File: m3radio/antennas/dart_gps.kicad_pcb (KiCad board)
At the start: 2 copper layers, 138 x 93 mm, 5 parts

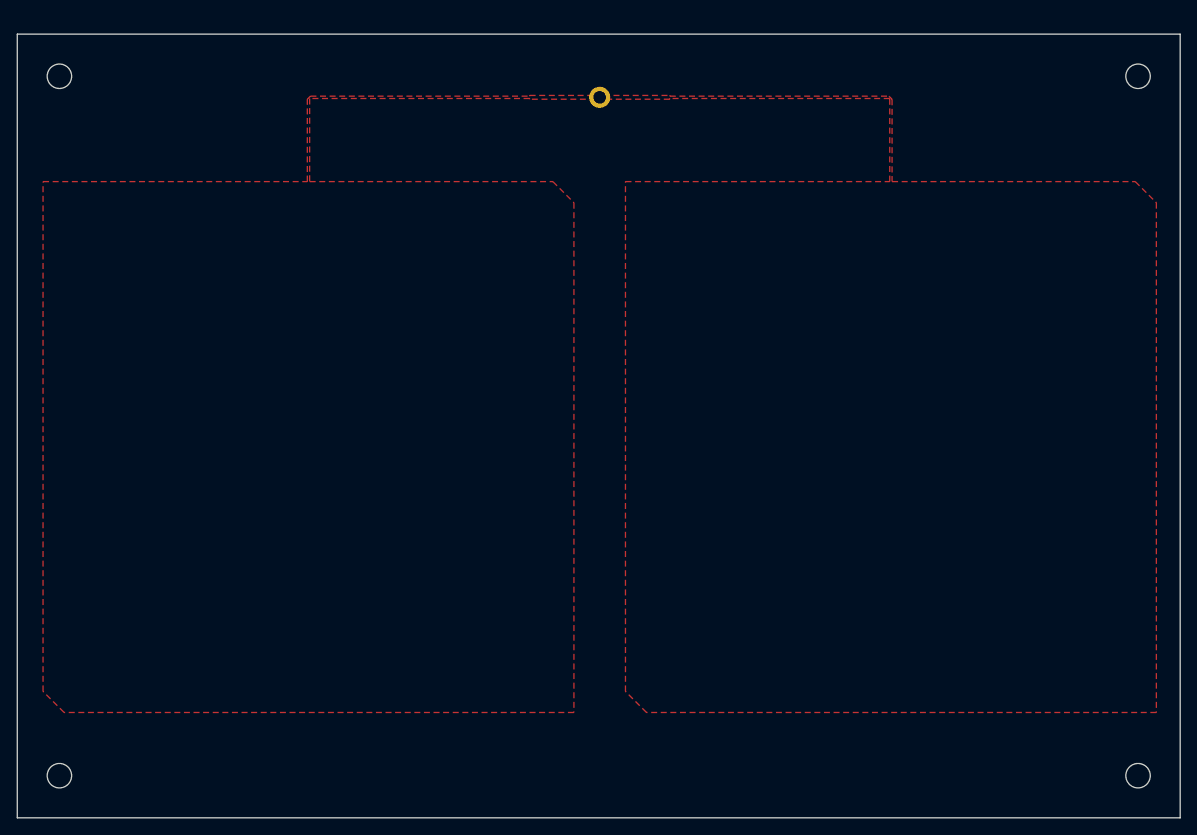
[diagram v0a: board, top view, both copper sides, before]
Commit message: make smaller dart antenna cutouts to ease manufacture
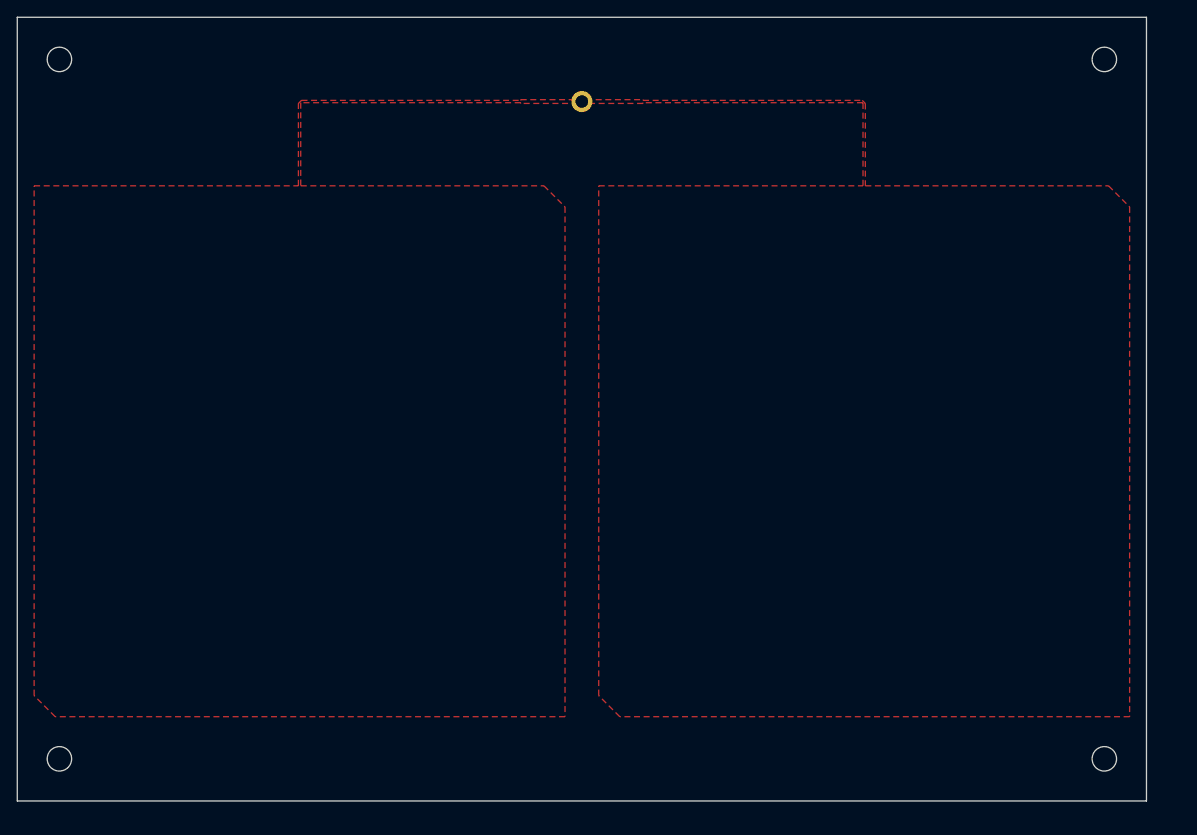
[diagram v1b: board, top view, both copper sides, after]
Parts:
- moved ? 4.47 mm to (149.0, 173.0)
- moved ? 4.47 mm to (149.0, 256.0)
- moved ? 2.17 mm to (87.0, 178.0)
- moved ? 2.00 mm to (25.0, 256.0)
- moved ? 2.00 mm to (25.0, 173.0)
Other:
- board size 138 x 93 mm -> 134 x 93 mm
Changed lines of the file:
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@@
-(kicad_pcb (version 20160815) (host pcbnew no-vcs-found-7520~57~ubuntu14.04.1)
+(kicad_pcb (version 20170123) (host pcbnew no-vcs-found-7587~57~ubuntu14.04.1)
   (general
-    (links 0)
-    (no_connects 0)
-    (area 19.949999 169.949999 158.050001 263.050001)
+    (links 1)
+    (no_connects 1)
+    (area 19.949999 167.949999 154.050001 261.050001)
     (thickness 1.6)
     (drawings 4)
@@
   (layers
     (0 F.Cu signal)
-    (31 B.Cu signal hide)
+    (31 B.Cu signal)
     (40 Dwgs.User user)
     (44 Edge.Cuts user)
@@
       (psnegative false)
       (psa4output false)
-      (plotreference true)
-      (plotvalue true)
+      (plotreference false)
+      (plotvalue false)
       (plotinvisibletext false)
       (padsonsilk false)
@@
   )
   (module X1 (layer F.Cu)
-    (at 153 175)
+    (at 87 178)
+    (fp_text reference "" (at 0 0) (layer F.SilkS)
+      (effects (font (thickness 0.15)))
+    )
+    (fp_text value "" (at 0 0) (layer F.SilkS)
+      (effects (font (thickness 0.15)))
+    )
+    (pad 1 thru_hole circle (at 0 0) (size 2.5 2.5) (drill 1.5) (layers F.Cu)
+      (net 1 Antennas) (zone_connect 2))
+  )
+  (module X1 (layer F.Cu)
+    (at 149 173)
     (fp_text reference "" (at 0 0) (layer F.SilkS)
       (effects (font (thickness 0.15)))
@@
   )
   (module X1 (layer F.Cu)
-    (at 153 258)
+    (at 149 256)
     (fp_text reference "" (at 0 0) (layer F.SilkS)
       (effects (font (thickness 0.15)))
@@
   )
   (module X1 (layer F.Cu)
-    (at 25 258)
+    (at 25 256)
     (fp_text reference "" (at 0 0) (layer F.SilkS)
       (effects (font (thickness 0.15)))
@@
   )
   (module X1 (layer F.Cu)
-    (at 25 175)
+    (at 25 173)
     (fp_text reference "" (at 0 0) (layer F.SilkS)
       (effects (font (thickness 0.15)))
@@
       (zone_connect 2))
   )
-  (module X1 (layer F.Cu)
-    (at 89.115 177.5)
-    (fp_text reference "" (at 0 0) (layer F.SilkS)
-      (effects (font (thickness 0.15)))
-    )
-    (fp_text value "" (at 0 0) (layer F.SilkS)
-      (effects (font (thickness 0.15)))
-    )
-    (pad 1 thru_hole circle (at 0 0) (size 2.5 2.5) (drill 1.5) (layers F.Cu)
-      (net 1 Antennas) (zone_connect 2))
-  )
-  (gr_line (start 20 263) (end 20 170) (layer Edge.Cuts) (width 0.1))
-  (gr_line (start 20 170) (end 158 170) (layer Edge.Cuts) (width 0.1))
-  (gr_line (start 158 170) (end 158 263) (layer Edge.Cuts) (width 0.1))
-  (gr_line (start 158 263) (end 20 263) (layer Edge.Cuts) (width 0.1))
+  (gr_line (start 20 261) (end 20 168) (layer Edge.Cuts) (width 0.1))
+  (gr_line (start 20 168) (end 154 168) (layer Edge.Cuts) (width 0.1))
+  (gr_line (start 154 168) (end 154 261) (layer Edge.Cuts) (width 0.1))
+  (gr_line (start 154 261) (end 20 261) (layer Edge.Cuts) (width 0.1))
   (zone (net 1) (net_name Antennas) (layer F.Cu) (hatch edge 0.5)
     (connect_pads (clearance 0.3))
@@
     (polygon
       (pts
-        (xy 89.615 177.276) (xy 97.4326 177.276) (xy 97.4326 177.3625) (xy 123.4451 177.3625) (xy 123.8101 177.7274)
-        (xy 123.8101 187.5) (xy 152.6726 187.5) (xy 155.1726 190) (xy 155.1726 250.5) (xy 94.6726 250.5)
-        (xy 92.1726 248) (xy 92.1726 187.5) (xy 123.5351 187.5) (xy 123.5351 177.6375) (xy 97.4326 177.6375)
-        (xy 97.4326 177.724) (xy 89.615 177.724) (xy 89.615 178) (xy 88.615 178) (xy 88.615 177.724)
-        (xy 80.7975 177.724) (xy 80.7975 177.6375) (xy 54.695 177.6375) (xy 54.695 187.5) (xy 83.5575 187.5)
-        (xy 86.0575 190) (xy 86.0575 250.5) (xy 25.5575 250.5) (xy 23.0575 248) (xy 23.0575 187.5)
-        (xy 54.42 187.5) (xy 54.42 177.7274) (xy 54.7849 177.3625) (xy 80.7975 177.3625) (xy 80.7975 177.276)
-        (xy 88.615 177.276) (xy 88.615 177) (xy 89.615 177)
+        (xy 87.5 177.776) (xy 94.26 177.776) (xy 94.26 177.8625) (xy 120.2726 177.8625) (xy 120.6375 178.2274)
+        (xy 120.6375 188) (xy 149.5 188) (xy 152 190.5) (xy 152 251) (xy 91.5 251)
+        (xy 89 248.5) (xy 89 188) (xy 120.3625 188) (xy 120.3625 178.1375) (xy 94.26 178.1375)
+        (xy 94.26 178.224) (xy 87.5 178.224) (xy 87.5 178.5) (xy 86.5 178.5) (xy 86.5 178.224)
+        (xy 79.74 178.224) (xy 79.74 178.1375) (xy 53.6375 178.1375) (xy 53.6375 188) (xy 82.5 188)
+        (xy 85 190.5) (xy 85 251) (xy 24.5 251) (xy 22 248.5) (xy 22 188)
+        (xy 53.3625 188) (xy 53.3625 178.2274) (xy 53.7274 177.8625) (xy 79.74 177.8625) (xy 79.74 177.776)
+        (xy 86.5 177.776) (xy 86.5 177.5) (xy 87.5 177.5)
       )
     )
